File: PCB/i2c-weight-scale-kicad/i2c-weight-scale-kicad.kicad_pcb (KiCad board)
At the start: 2 copper layers, 43 x 49 mm, 14 parts, among them J1 I2C_RJ14, P1 4_STRAIN_GAUGES, U1 INA126, U2 PIC12F1822

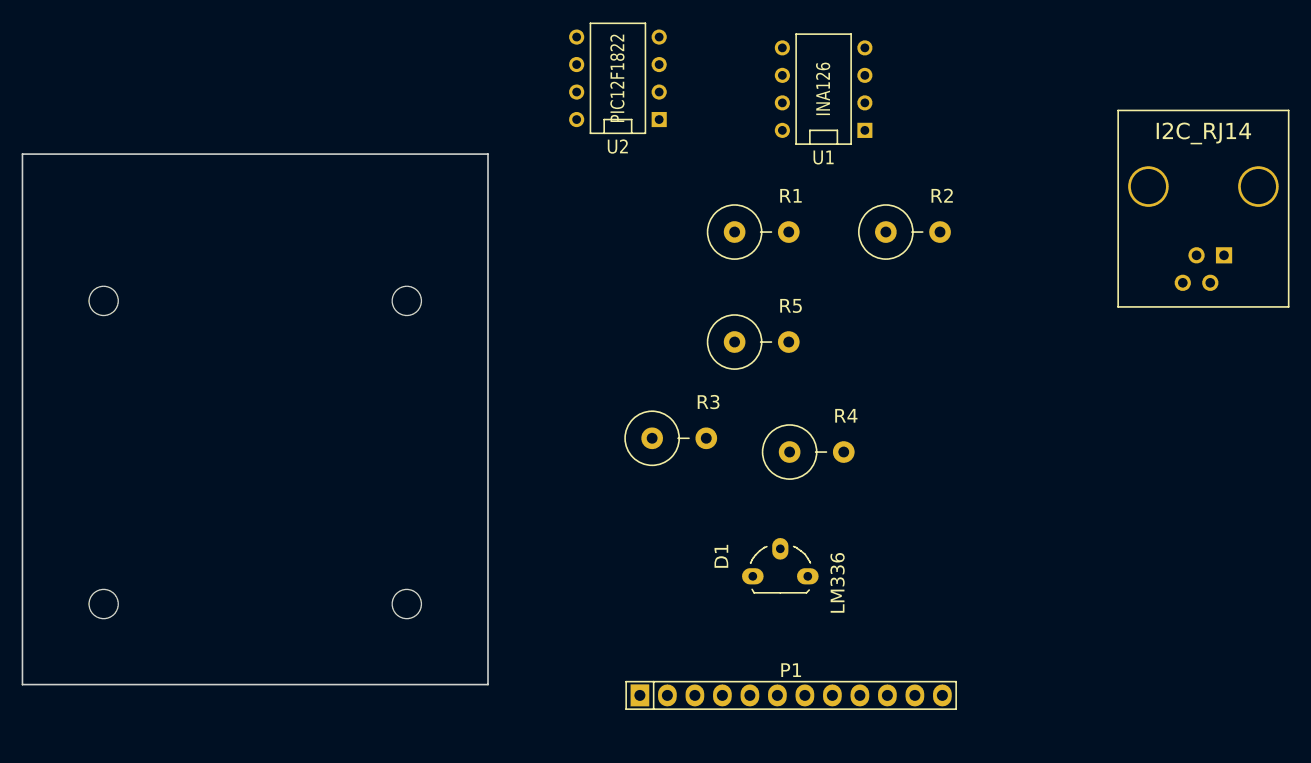
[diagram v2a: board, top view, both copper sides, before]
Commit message: Rough footprint placements on the PCB
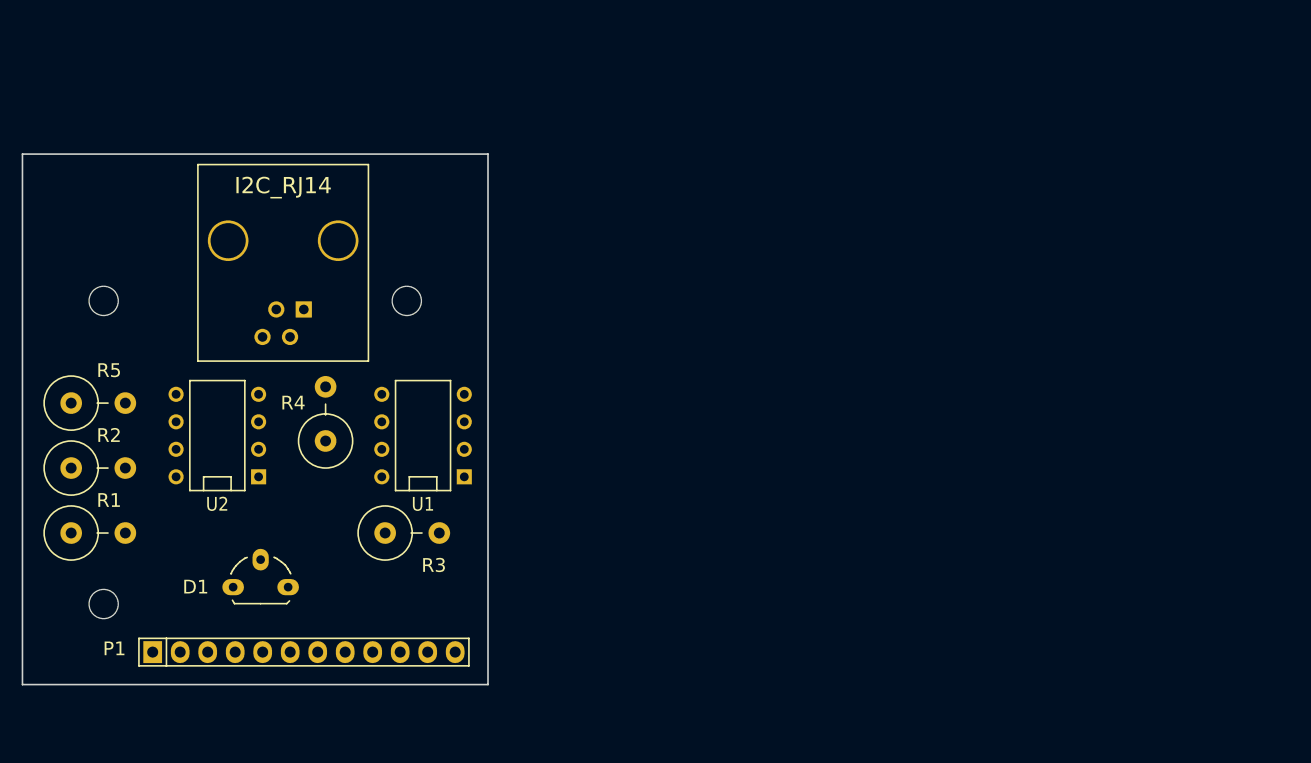
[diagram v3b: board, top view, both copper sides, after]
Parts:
- removed the MH at (85.5, 91.6)
- moved J1 85.1 mm to (69.0, 58.0)
- moved R2 78.3 mm to (57.0, 79.0)
- moved R1 67.3 mm to (57.0, 85.0)
- moved R5 61.5 mm to (57.0, 73.0)
- moved U2 49.6 mm to (68.0, 76.0)
- moved U1 48.9 mm to (87.0, 76.0)
- moved D1 48.0 mm to (72.0, 90.0)
- moved R4 45.5 mm to (78.0, 74.0), turned to 90 degrees
- moved P1 45.2 mm to (76.0, 96.0)
- moved R3 26.2 mm to (86.0, 85.0)
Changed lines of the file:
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@@
     (links 26)
     (no_connects 26)
-    (area 0 0 0 0)
+    (area 31.86523 49.924999 111.33289 99.075001)
     (thickness 1.6)
     (drawings 4)
     (tracks 0)
     (zones 0)
-    (modules 14)
+    (modules 13)
     (nets 20)
   )
@@
   )
   (module Housings_TO-92:TO-92-Free-molded-wide-oval (layer F.Cu)
-    (at 120 89 90)
+    (at 72 90 90)
     (descr "TO-92 allgemein free molded wide oval drill 0,8mm")
     (tags "TO-92 allgemein free molded wide oval drill 0,8mm")
-    (fp_text reference D1 (at 1.8415 -5.3975 90) (layer F.SilkS)
-      (effects (font (thickness 0.3048)))
-    )
-    (fp_text value LM336 (at -0.635 5.334 90) (layer F.SilkS)
+    (fp_text reference D1 (at 0 -6 180) (layer F.SilkS)
+      (effects (font (thickness 0.3048)))
+    )
+    (fp_text value LM336 (at 2 5 90) (layer F.SilkS) hide
       (effects (font (thickness 0.3048)))
     )
@@
   )
   (module Pin_Headers:Pin_Header_Straight_1x12 (layer F.Cu)
-    (at 121 100)
+    (at 76 96)
     (descr "Through hole pin header")
     (tags "pin header")
-    (fp_text reference P1 (at 0 -2.286) (layer F.SilkS)
+    (fp_text reference P1 (at -17.5 -0.3) (layer F.SilkS)
       (effects (font (size 1.27 1.27) (thickness 0.2032)))
     )
@@
   )
   (module Resistors_ThroughHole:Resistor_Vertical_RM5mm (layer F.Cu)
-    (at 118.28 57.2)
+    (at 57 85)
     (descr "Resistor, Vertical, RM 5mm, 1/3W,")
     (tags "Resistor, Vertical, RM 5mm, 1/3W,")
-    (fp_text reference R1 (at 2.70002 -3.29946) (layer F.SilkS)
+    (fp_text reference R1 (at 1 -3) (layer F.SilkS)
       (effects (font (thickness 0.3048)))
     )
@@
   )
   (module Resistors_ThroughHole:Resistor_Vertical_RM5mm (layer F.Cu)
-    (at 132.25 57.2)
+    (at 57 79)
     (descr "Resistor, Vertical, RM 5mm, 1/3W,")
     (tags "Resistor, Vertical, RM 5mm, 1/3W,")
-    (fp_text reference R2 (at 2.70002 -3.29946) (layer F.SilkS)
+    (fp_text reference R2 (at 1 -3) (layer F.SilkS)
       (effects (font (thickness 0.3048)))
     )
@@
   )
   (module Resistors_ThroughHole:Resistor_Vertical_RM5mm (layer F.Cu)
-    (at 110.66 76.25)
+    (at 86 85)
     (descr "Resistor, Vertical, RM 5mm, 1/3W,")
     (tags "Resistor, Vertical, RM 5mm, 1/3W,")
-    (fp_text reference R3 (at 2.70002 -3.29946) (layer F.SilkS)
+    (fp_text reference R3 (at 2 3) (layer F.SilkS)
       (effects (font (thickness 0.3048)))
     )
@@
   )
   (module Resistors_ThroughHole:Resistor_Vertical_RM5mm (layer F.Cu)
-    (at 123.36 77.52)
+    (at 78 74 90)
     (descr "Resistor, Vertical, RM 5mm, 1/3W,")
     (tags "Resistor, Vertical, RM 5mm, 1/3W,")
-    (fp_text reference R4 (at 2.70002 -3.29946) (layer F.SilkS)
-      (effects (font (thickness 0.3048)))
-    )
-    (fp_text value 1K (at 0 4.50088) (layer F.SilkS) hide
+    (fp_text reference R4 (at 1 -3 180) (layer F.SilkS)
+      (effects (font (thickness 0.3048)))
+    )
+    (fp_text value 1K (at 0 4.50088 90) (layer F.SilkS) hide
       (effects (font (size 1.50114 1.50114) (thickness 0.20066)))
     )
     (fp_line (start -0.09906 0) (end 0.9017 0) (layer F.SilkS) (width 0.15))
     (fp_circle (center -2.49936 0) (end 0 0) (layer F.SilkS) (width 0.15))
-    (pad 1 thru_hole circle (at -2.49936 0) (size 1.99898 1.99898) (drill 1.00076) (layers *.Cu *.SilkS *.Mask)
+    (pad 1 thru_hole circle (at -2.49936 0 90) (size 1.99898 1.99898) (drill 1.00076) (layers *.Cu *.SilkS *.Mask)
       (net 16 "Net-(R4-Pad1)"))
-    (pad 2 thru_hole circle (at 2.5019 0) (size 1.99898 1.99898) (drill 1.00076) (layers *.Cu *.SilkS *.Mask)
+    (pad 2 thru_hole circle (at 2.5019 0 90) (size 1.99898 1.99898) (drill 1.00076) (layers *.Cu *.SilkS *.Mask)
       (net 3 GND))
   )
   (module Resistors_ThroughHole:Resistor_Vertical_RM5mm (layer F.Cu)
-    (at 118.28 67.36)
+    (at 57 73)
     (descr "Resistor, Vertical, RM 5mm, 1/3W,")
     (tags "Resistor, Vertical, RM 5mm, 1/3W,")
-    (fp_text reference R5 (at 2.70002 -3.29946) (layer F.SilkS)
+    (fp_text reference R5 (at 1 -3) (layer F.SilkS)
       (effects (font (thickness 0.3048)))
     )
@@
   )
   (module Sockets_DIP:DIP-8__300 (layer F.Cu)
-    (at 124 44 90)
+    (at 87 76 90)
     (descr "8 pins DIL package, round pads")
     (tags DIL)
@@
       (effects (font (size 1.27 1.143) (thickness 0.2032)))
     )
-    (fp_text value INA126 (at 0 0 90) (layer F.SilkS)
+    (fp_text value INA126 (at 0 0 90) (layer F.SilkS) hide
       (effects (font (size 1.27 1.016) (thickness 0.2032)))
     )
@@
   )
   (module Sockets_DIP:DIP-8__300 (layer F.Cu)
-    (at 105 43 90)
+    (at 68 76 90)
     (descr "8 pins DIL package, round pads")
     (tags DIL)
@@
       (effects (font (size 1.27 1.143) (thickness 0.2032)))
     )
-    (fp_text value PIC12F1822 (at 0 0 90) (layer F.SilkS)
+    (fp_text value PIC12F1822 (at 0 0 90) (layer F.SilkS) hide
       (effects (font (size 1.27 1.016) (thickness 0.2032)))
     )
@@
   )
   (module simlun:RJ14_6P4C_right_angle_Molex_95009-7641 (layer F.Cu)
-    (at 154 53)
+    (at 69 58)
     (fp_text reference J1 (at 5.08 13.97) (layer F.SilkS) hide
       (effects (font (size 1.5 1.5) (thickness 0.15)))
@@
     (descr "Mounting hole, Befestigungsbohrung, 2,7mm, No Annular, Kein Restring,")
     (tags "Mounting hole, Befestigungsbohrung, 2,7mm, No Annular, Kein Restring,")
-    (fp_text reference MH (at 0 -4.0005) (layer F.SilkS) hide
-      (effects (font (thickness 0.3048)))
-    )
-    (fp_text value MountingHole_2-7mm_RevA_Date21Jun2010 (at 0.09906 3.59918) (layer F.SilkS) hide
-      (effects (font (thickness 0.3048)))
-    )
-    (fp_circle (center 0 0) (end 2.70002 0) (layer Cmts.User) (width 0.381))
-    (pad 1 thru_hole circle (at 0 0) (size 2.70002 2.70002) (drill 2.70002) (layers))
-  )
-  (module Mounting_Holes:MountingHole_2-7mm (layer F.Cu)
-    (at 85.5 91.56)
-    (descr "Mounting hole, Befestigungsbohrung, 2,7mm, No Annular, Kein Restring,")
-    (tags "Mounting hole, Befestigungsbohrung, 2,7mm, No Annular, Kein Restring,")

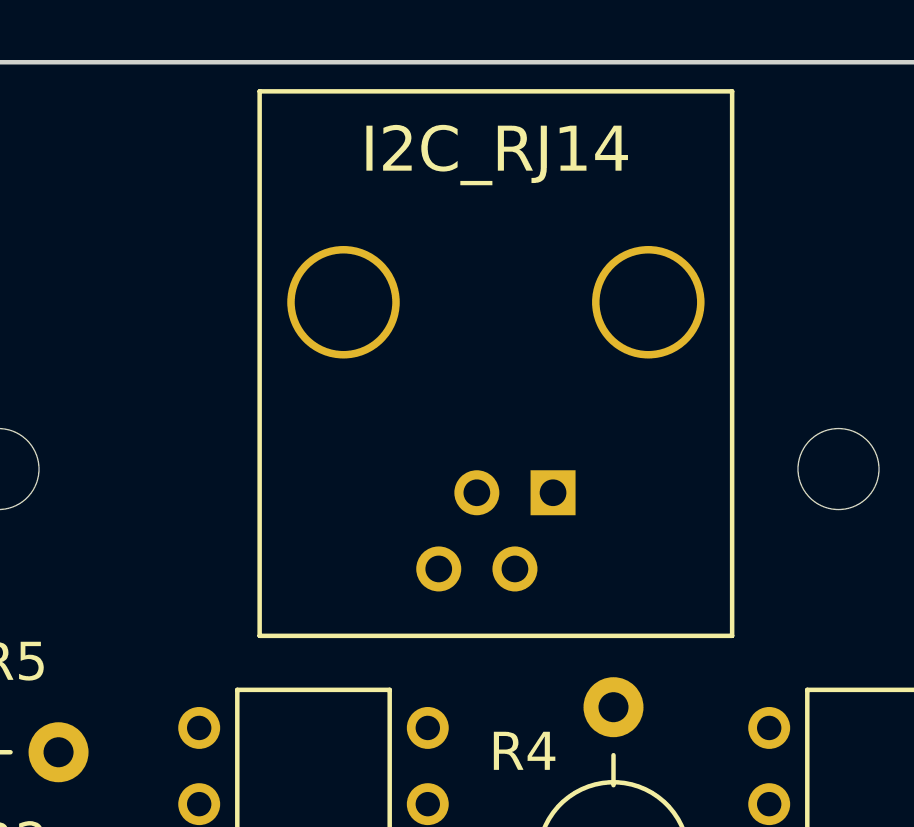
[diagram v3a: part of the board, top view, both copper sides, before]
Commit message: Place the RJ14 connector on the PCB
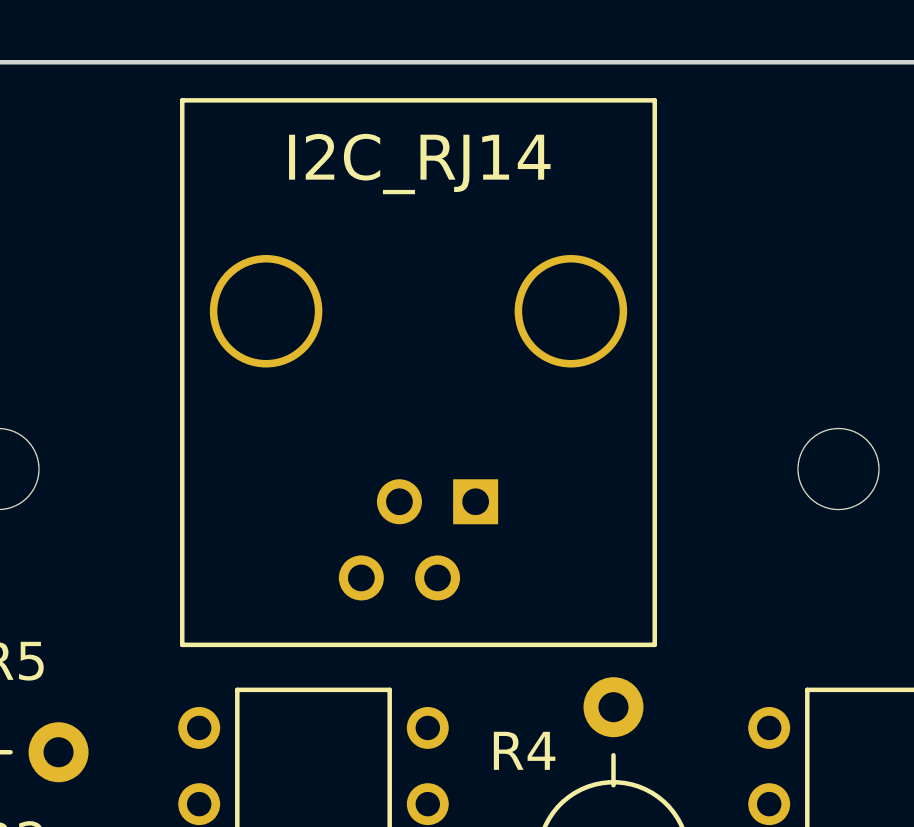
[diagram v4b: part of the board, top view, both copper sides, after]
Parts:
- moved J1 8.61 mm to (63.6, 51.3)
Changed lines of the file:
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@@
     (links 26)
     (no_connects 26)
-    (area 31.86523 49.924999 111.33289 99.075001)
+    (area 31.86523 49.924999 111.33289 131.454001)
     (thickness 1.6)
     (drawings 4)
@@
     )
   )
-  (module simlun:RJ14_6P4C_right_angle_Molex_95009-7641 (layer F.Cu)
-    (at 69 58)
-    (fp_text reference J1 (at 5.08 13.97) (layer F.SilkS) hide
-      (effects (font (size 1.5 1.5) (thickness 0.15)))
-    )
-    (fp_text value I2C_RJ14 (at 5.08 -5.08) (layer F.SilkS)
-      (effects (font (size 1.5 1.5) (thickness 0.15)))
-    )
-    (fp_line (start -2.795 11.12) (end 12.955 11.12) (layer F.SilkS) (width 0.15))
-    (fp_line (start -2.795 -7.03) (end 12.955 -7.03) (layer F.SilkS) (width 0.15))
-    (fp_line (start 12.955 -7.03) (end 12.955 11.12) (layer F.SilkS) (width 0.15))
-    (fp_line (start -2.795 -7.03) (end -2.795 11.12) (layer F.SilkS) (width 0.15))
-    (pad "" np_thru_hole circle (at 0 0) (size 3.75 3.75) (drill 3.25) (layers *.Cu *.SilkS *.Mask))
-    (pad "" np_thru_hole circle (at 10.16 0) (size 3.75 3.75) (drill 3.25) (layers *.Cu *.SilkS *.Mask))
-    (pad 4 thru_hole circle (at 3.175 8.89) (size 1.5 1.5) (drill 0.89) (layers *.Cu *.Mask F.SilkS)
-      (net 4 "Net-(J1-Pad4)"))
-    (pad 3 thru_hole circle (at 4.445 6.35) (size 1.5 1.5) (drill 0.89) (layers *.Cu *.Mask F.SilkS)
-      (net 5 "Net-(J1-Pad3)"))
-    (pad 2 thru_hole circle (at 5.715 8.89) (size 1.5 1.5) (drill 0.89) (layers *.Cu *.Mask F.SilkS)
-      (net 3 GND))
-    (pad 1 thru_hole rect (at 6.985 6.35) (size 1.5 1.5) (drill 0.89) (layers *.Cu *.Mask F.SilkS)
-      (net 6 VDD))
-  )
   (module Mounting_Holes:MountingHole_2-7mm (layer F.Cu)
     (at 57.5 63.56)
@@
     (pad 1 thru_hole circle (at 0 0) (size 2.70002 2.70002) (drill 2.70002) (layers))
   )
+  (module simlun:RJ14_6P4C_right_angle_Molex_95009-7641 locked (layer F.Cu)
+    (at 63.625 51.27)
+    (fp_text reference J1 (at 7.875 21) (layer F.SilkS) hide
+      (effects (font (size 1.5 1.5) (thickness 0.15)))
+    )
+    (fp_text value I2C_RJ14 (at 7.875 1.95) (layer F.SilkS)
+      (effects (font (size 1.5 1.5) (thickness 0.15)))
+    )
+    (fp_line (start 0 18.15) (end 15.75 18.15) (layer F.SilkS) (width 0.15))
+    (fp_line (start 0 0) (end 15.75 0) (layer F.SilkS) (width 0.15))
+    (fp_line (start 15.75 0) (end 15.75 18.15) (layer F.SilkS) (width 0.15))
+    (fp_line (start 0 0) (end 0 18.15) (layer F.SilkS) (width 0.15))
+    (pad "" np_thru_hole circle (at 2.795 7.03) (size 3.75 3.75) (drill 3.25) (layers *.Cu *.SilkS *.Mask))
+    (pad "" np_thru_hole circle (at 12.955 7.03) (size 3.75 3.75) (drill 3.25) (layers *.Cu *.SilkS *.Mask))
+    (pad 4 thru_hole circle (at 5.97 15.92) (size 1.5 1.5) (drill 0.89) (layers *.Cu *.Mask F.SilkS)
+      (net 4 "Net-(J1-Pad4)"))
+    (pad 3 thru_hole circle (at 7.24 13.38) (size 1.5 1.5) (drill 0.89) (layers *.Cu *.Mask F.SilkS)
+      (net 5 "Net-(J1-Pad3)"))
+    (pad 2 thru_hole circle (at 8.51 15.92) (size 1.5 1.5) (drill 0.89) (layers *.Cu *.Mask F.SilkS)
+      (net 3 GND))
+    (pad 1 thru_hole rect (at 9.78 13.38) (size 1.5 1.5) (drill 0.89) (layers *.Cu *.Mask F.SilkS)
+      (net 6 VDD))
+  )
   (gr_line (start 50 99) (end 50 50) (angle 90) (layer Edge.Cuts) (width 0.15))

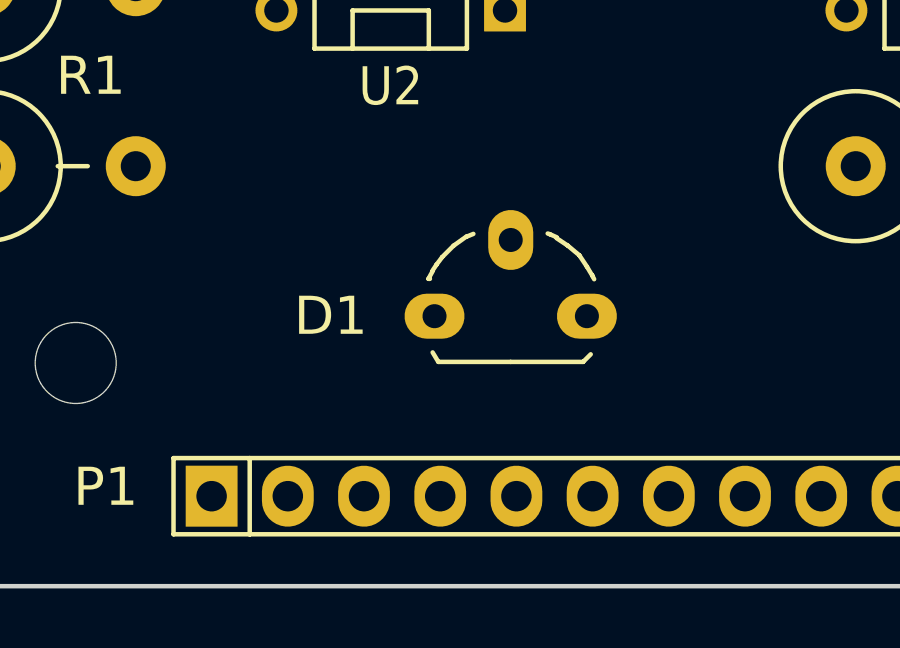
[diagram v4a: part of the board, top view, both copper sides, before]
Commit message: Move origins to upper left corner of PCB
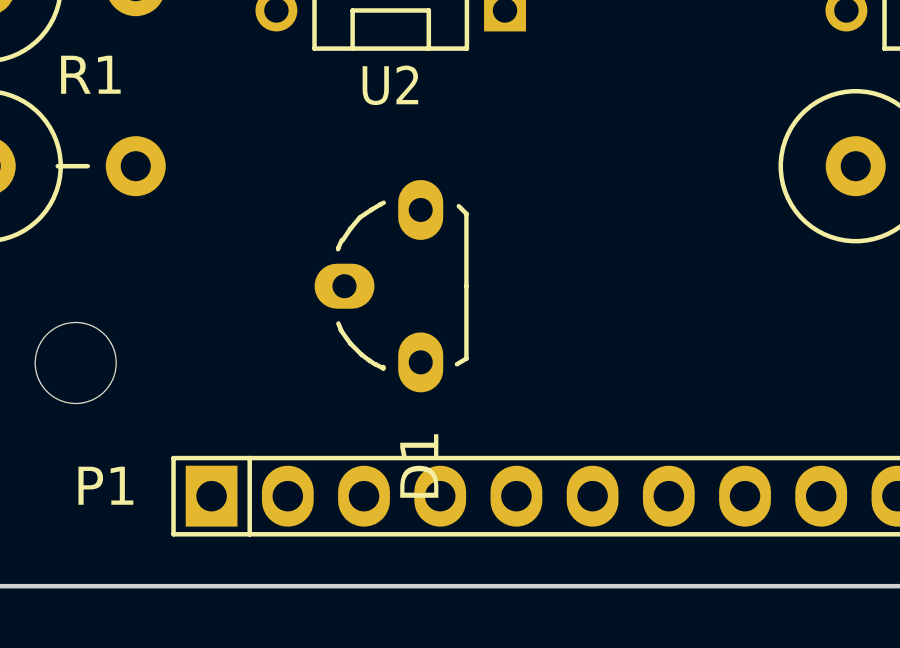
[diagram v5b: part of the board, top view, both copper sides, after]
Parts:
- moved D1 3.16 mm to (69.0, 89.0), turned to 180 degrees
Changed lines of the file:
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@@
     (pad_drill 0.89)
     (pad_to_mask_clearance 0.2)
-    (aux_axis_origin 0 0)
+    (aux_axis_origin 50 50)
+    (grid_origin 50 50)
     (visible_elements FFFFFF7F)
     (pcbplotparams
@@
   )
   (module Housings_TO-92:TO-92-Free-molded-wide-oval (layer F.Cu)
-    (at 72 90 90)
+    (at 69 89 180)
     (descr "TO-92 allgemein free molded wide oval drill 0,8mm")
     (tags "TO-92 allgemein free molded wide oval drill 0,8mm")
-    (fp_text reference D1 (at 0 -6 180) (layer F.SilkS)
+    (fp_text reference D1 (at 0 -6 270) (layer F.SilkS)
       (effects (font (thickness 0.3048)))
     )
-    (fp_text value LM336 (at 2 5 90) (layer F.SilkS) hide
+    (fp_text value LM336 (at 2 5 180) (layer F.SilkS) hide
       (effects (font (thickness 0.3048)))
     )
@@
     (fp_line (start -1.524 0) (end -1.524 2.413) (layer F.SilkS) (width 0.15))
     (fp_line (start -1.524 0) (end -1.524 -2.413) (layer F.SilkS) (width 0.15))
-    (pad 2 thru_hole oval (at 2.54 0 90) (size 1.99898 1.50114) (drill 0.8001) (layers *.Cu *.Mask F.SilkS)
+    (pad 2 thru_hole oval (at 2.54 0 180) (size 1.99898 1.50114) (drill 0.8001) (layers *.Cu *.Mask F.SilkS)
       (net 1 "Net-(D1-Pad2)"))
-    (pad 1 thru_hole oval (at 0 -2.54 90) (size 1.50114 1.99898) (drill 0.8001) (layers *.Cu *.Mask F.SilkS)
+    (pad 1 thru_hole oval (at 0 -2.54 180) (size 1.50114 1.99898) (drill 0.8001) (layers *.Cu *.Mask F.SilkS)
       (net 2 "Net-(D1-Pad1)"))
-    (pad 3 thru_hole oval (at 0 2.54 90) (size 1.50114 1.99898) (drill 0.8001) (layers *.Cu *.Mask F.SilkS)
+    (pad 3 thru_hole oval (at 0 2.54 180) (size 1.50114 1.99898) (drill 0.8001) (layers *.Cu *.Mask F.SilkS)
       (net 3 GND))
   )
